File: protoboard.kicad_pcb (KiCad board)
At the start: 2 copper layers, 99.8 x 110 mm, 40 parts, among them J1 ⊕, J101 a, J102 b, J103 c, J104 d, J105 e, J106 f, J107 g, J108 h, J109 i, J110 j, J111 k, J112 l, J113 m, J114 n, J115 o, J116 p, J117 q, J118 r, J119 s, J120 t, J121 u, J122 v, J123 w, J124 x, J2 ⊕, J3 ⊕, J4 ⊕, J5 ⊖, J6 ⊖, J7 ⊖, J8 ⊖

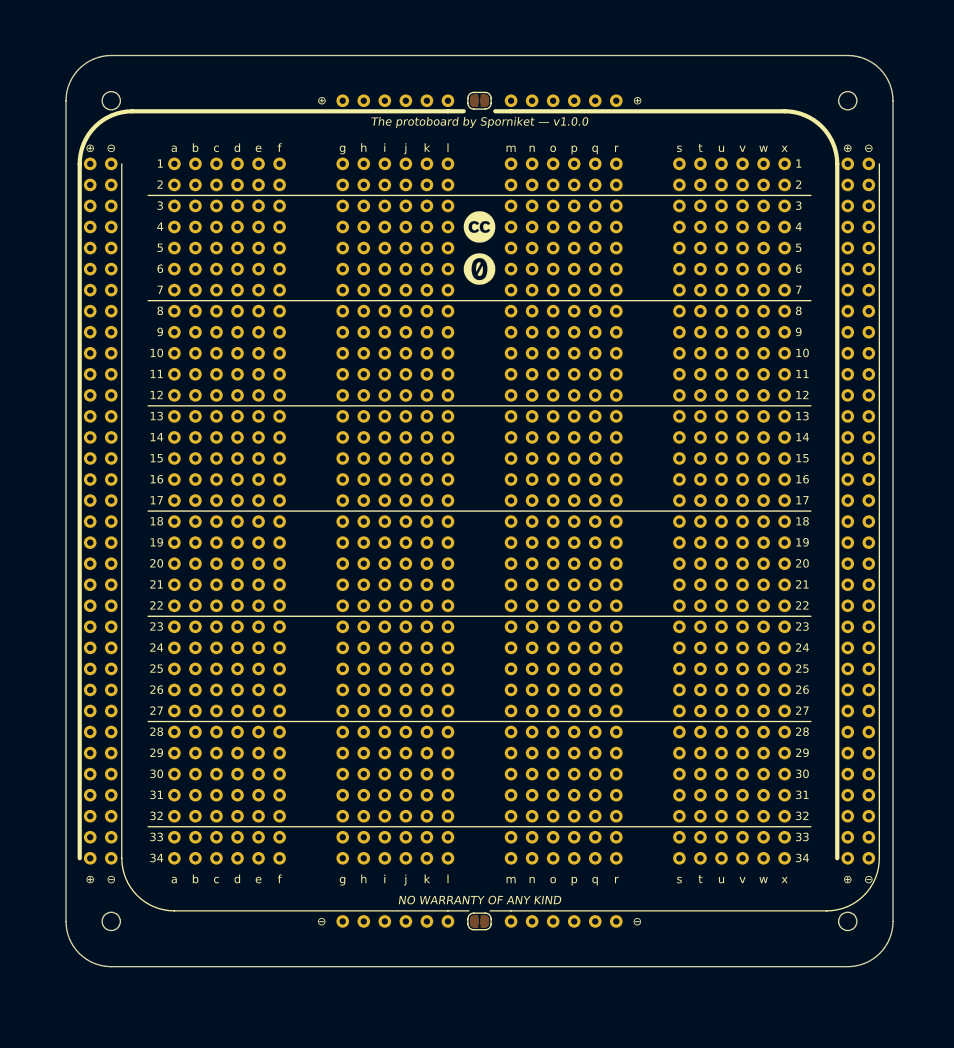
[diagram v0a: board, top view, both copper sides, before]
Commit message: wiring all the bussed connectors
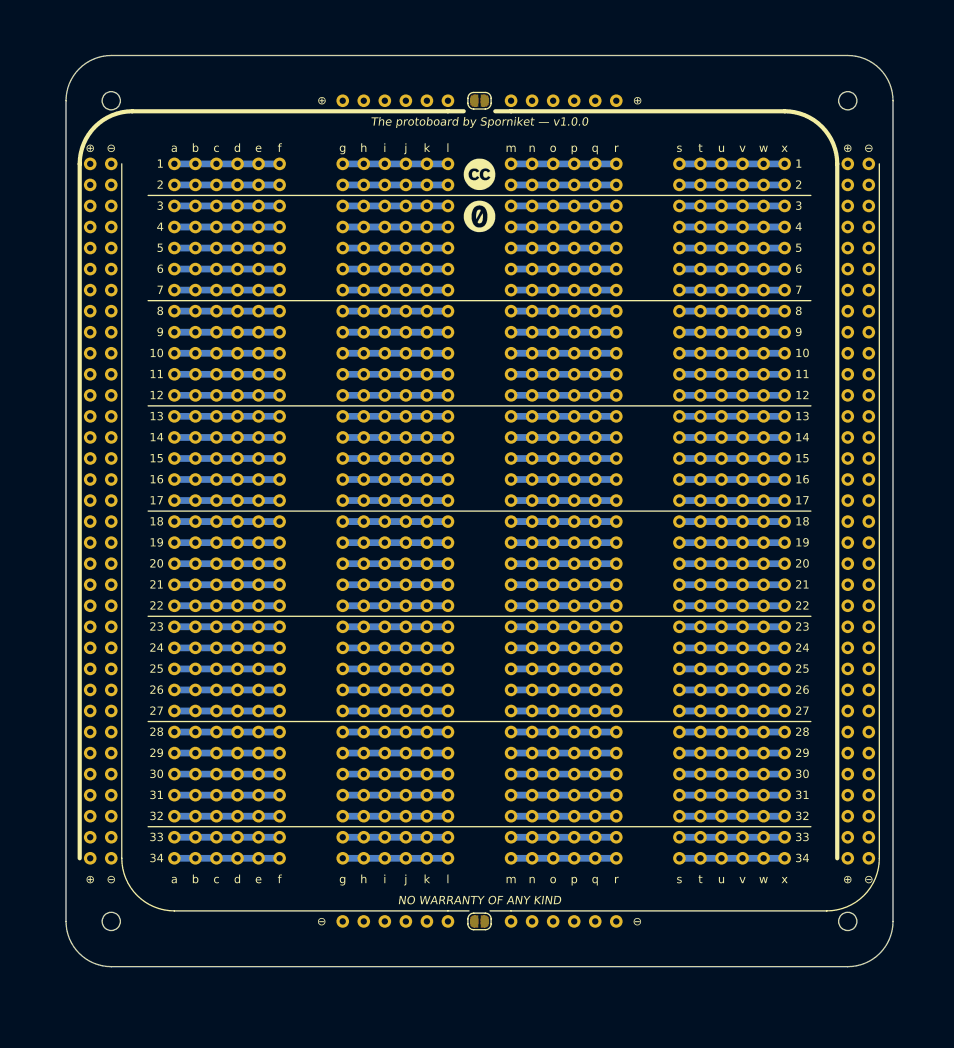
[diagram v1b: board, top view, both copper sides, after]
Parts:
- moved G*** 6.35 mm to (87.6, 82.5)
- moved G*** 6.35 mm to (87.6, 77.5)
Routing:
- net /C9: track 0.00 -> 12.7 mm
- net /C8: track 0.00 -> 12.7 mm
- net /C7: track 0.00 -> 12.7 mm
- net /C6: track 0.00 -> 12.7 mm
- net /C5: track 0.00 -> 12.7 mm
- net /C4: track 0.00 -> 12.7 mm
- net /C34: track 0.00 -> 12.7 mm
- net /C33: track 0.00 -> 12.7 mm
- net /C32: track 0.00 -> 12.7 mm
- net /C31: track 0.00 -> 12.7 mm
- net /C30: track 0.00 -> 12.7 mm
- net /C3: track 0.00 -> 12.7 mm
- net /C29: track 0.00 -> 12.7 mm
- net /C28: track 0.00 -> 12.7 mm
- net /C27: track 0.00 -> 12.7 mm
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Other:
- net class Default: clearance 0.2 -> 0.2032; trace_width 0.25 -> 0.8128; via_dia 0.8 -> 0.4064; via_drill 0.4 -> 0.2032
- rule trace_clearance: 0.2 -> 0.2032
- rule trace_min: 0.2 -> 0.2032
- rule via_min_drill: 0.3 -> 0.2032
- rule via_min_size: 0.4 -> 0.4064

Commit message: Adjust label contents and position, document annotation with actual repository
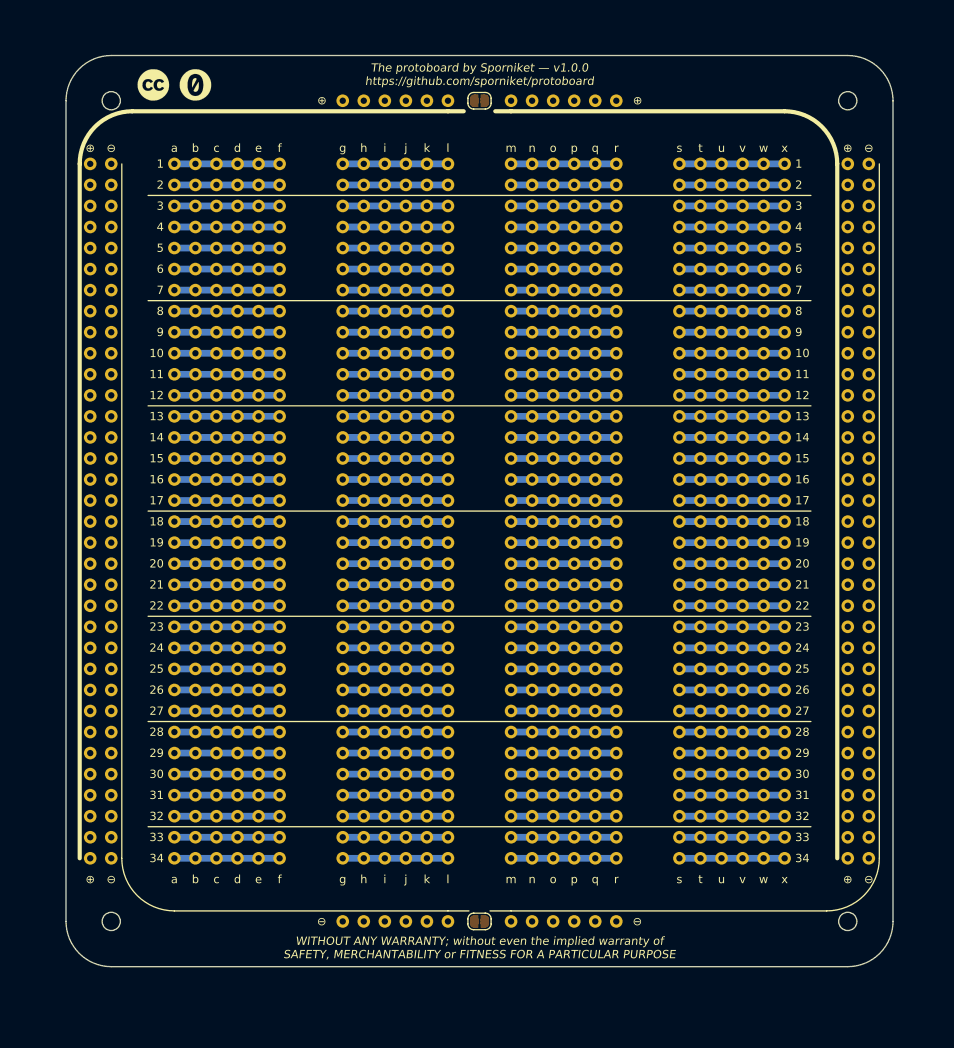
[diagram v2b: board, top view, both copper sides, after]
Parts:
- moved G*** 40.8 mm to (48.3, 66.7)
- moved G*** 37.8 mm to (53.3, 66.7)
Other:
- board text added: "The protoboard by Sporniket — v1.0.0 https://github.com/sporniket/protoboard"
- board text added: "WITHOUT ANY WARRANTY; without even the implied warranty of SAFETY, MERCHANTABILITY or FITNESS FOR A PARTICULAR PURPOSE"
- board text removed: "NO WARRANTY OF ANY KIND"
- board text removed: "The protoboard by Sporniket — v1.0.0"
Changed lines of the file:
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@@
     (date 2022-09-15)
     (company Sporniket)
+    (comment 2 "Original repository : https://github.com/sporniket/protoboard")
   )
   (layers
@@
   )
   (module cliparts:logo--cc--zero (layer F.Cu)
-    (at 87.63 82.55)
+    (at 53.34 66.675)
     (fp_text reference G*** (at 0 0) (layer F.SilkS) hide
       (effects (font (size 1.524 1.524) (thickness 0.3)))
@@
   )
   (module cliparts:logo--cc--cc (layer F.Cu)
-    (at 87.63 77.47)
+    (at 48.26 66.675)
     (fp_text reference G*** (at 0 0) (layer F.SilkS) hide
       (effects (font (size 1.524 1.524) (thickness 0.3)))
@@
     (pad 1 np_thru_hole circle (at 0 0) (size 2.2 2.2) (drill 2.2) (layers *.Cu *.Mask))
   )
-  (gr_text "NO WARRANTY OF ANY KIND" (at 87.63 165.1) (layer F.SilkS)
+  (gr_text "WITHOUT ANY WARRANTY; without even the implied warranty of\nSAFETY, MERCHANTABILITY or FITNESS FOR A PARTICULAR PURPOSE" (at 87.63 170.815) (layer F.SilkS)
     (effects (font (size 1 1) (thickness 0.15) italic))
   )
-  (gr_text "The protoboard by Sporniket — v1.0.0" (at 87.63 71.12) (layer F.SilkS)
+  (gr_text "The protoboard by Sporniket — v1.0.0\nhttps://github.com/sporniket/protoboard" (at 87.63 65.405) (layer F.SilkS)
     (effects (font (size 1 1) (thickness 0.15) italic))
   )

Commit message: copper pours for each power rail
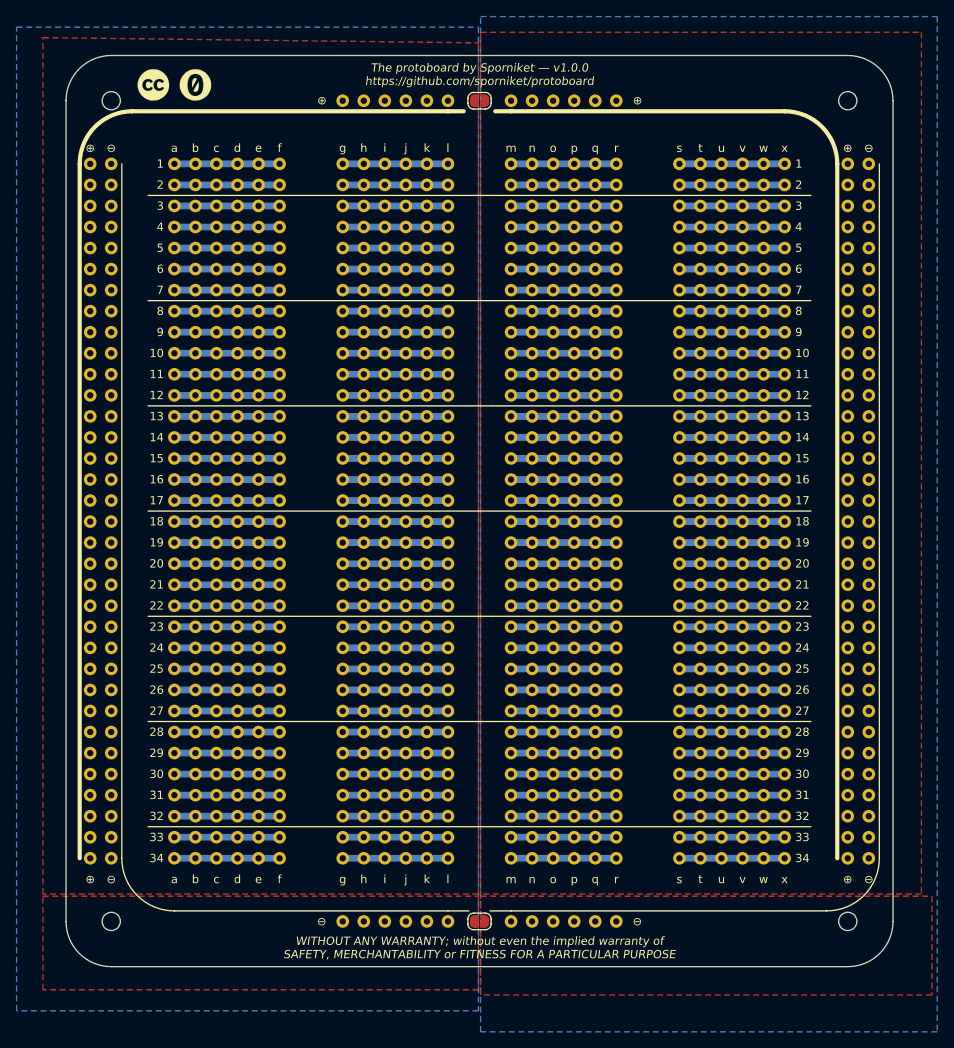
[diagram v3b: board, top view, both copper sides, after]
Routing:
- added copper zone on F.Cu, net Net-(J1-Pad1)
- added copper zone on F.Cu, net Net-(J3-Pad1)
- added copper zone on B.Cu, net Net-(J5-Pad1)
- added copper zone on F.Cu, net Net-(J5-Pad1)
- added copper zone on B.Cu, net Net-(J7-Pad1)
- added copper zone on F.Cu, net Net-(J7-Pad1)

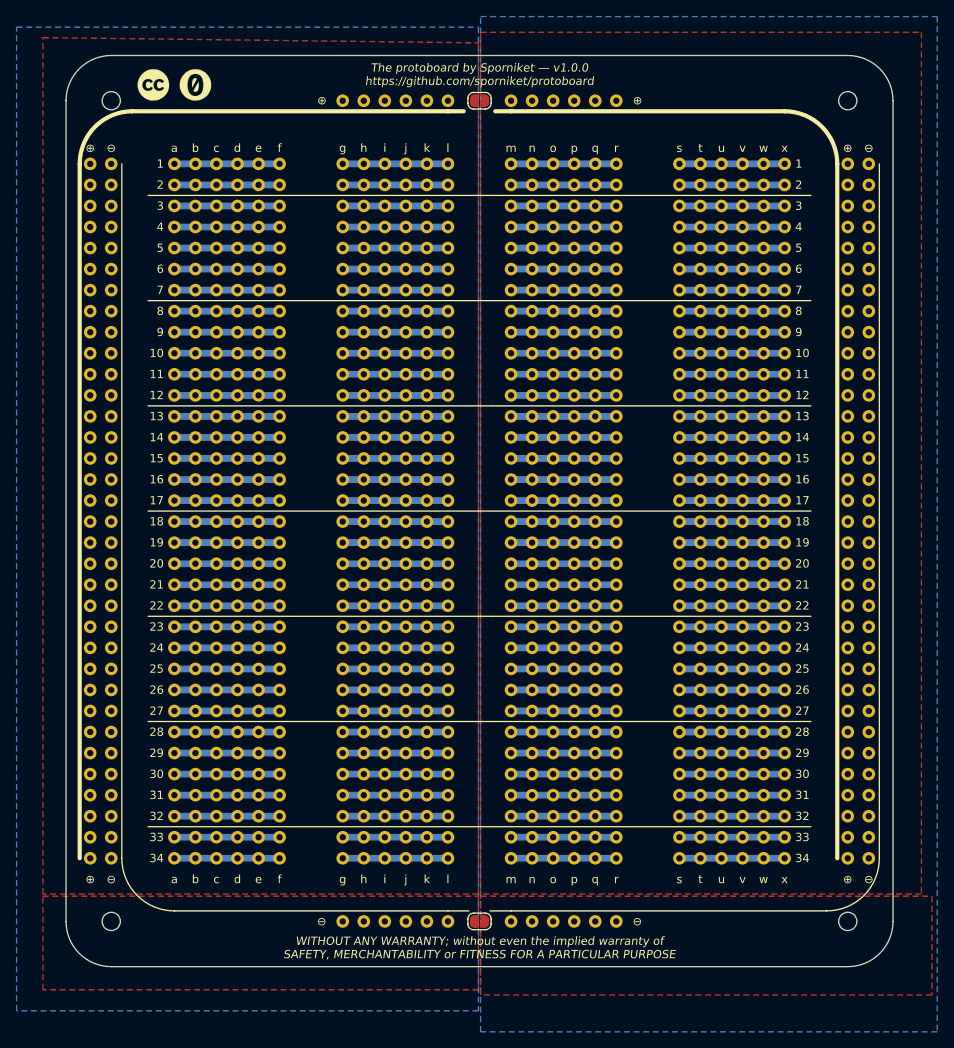
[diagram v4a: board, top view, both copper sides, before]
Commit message: migrate to Kicad 7
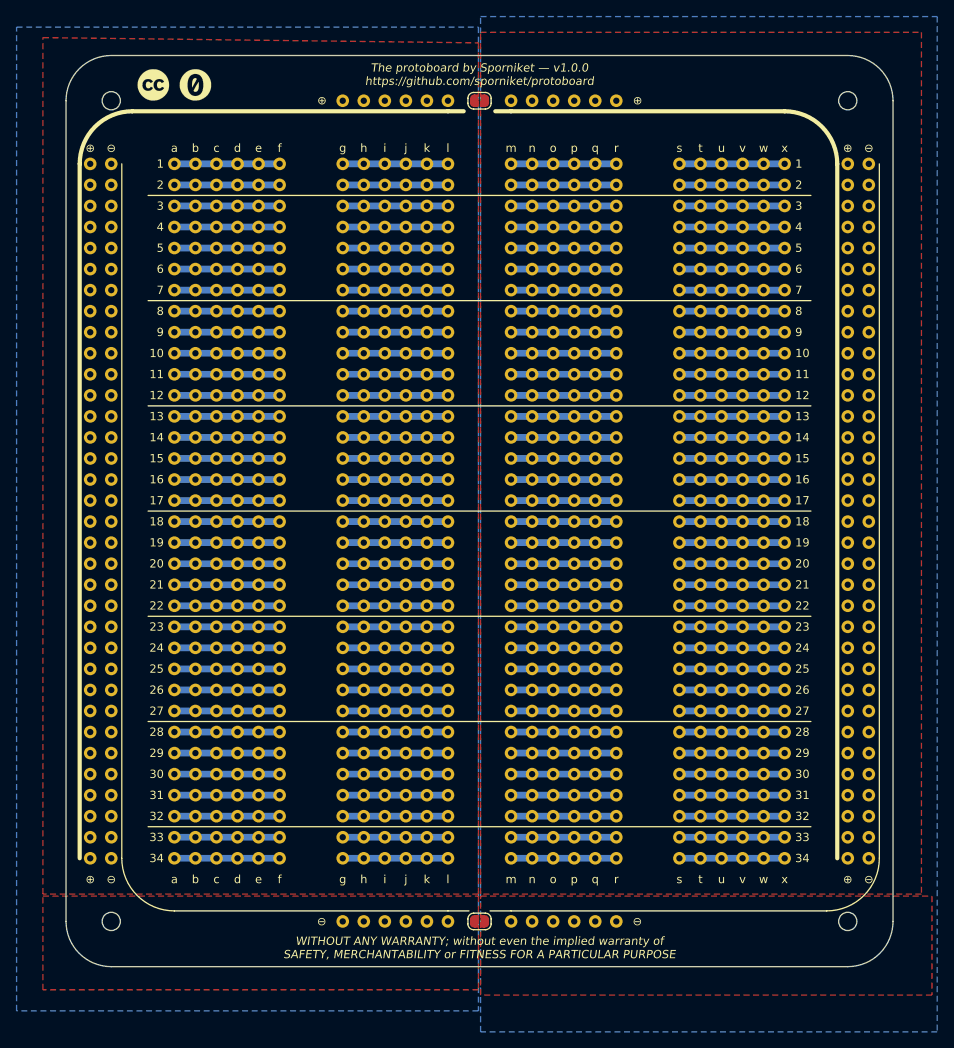
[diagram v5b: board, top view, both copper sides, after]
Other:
- net class Default removed
